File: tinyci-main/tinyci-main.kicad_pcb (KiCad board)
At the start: 2 copper layers, 110 x 82.5 mm, 54 parts, among them J1 Jack-DC, J2 Jack-DC, J3 Jack-DC, J4 Conn_01x13_Male, J5 Conn_01x13_Male, J6 Jack-DC, J7 Jack-DC, J8 Conn_01x06_Male, J9 Conn_01x06_Male, K1 SANYOU_SRD_Form_C, K2 SANYOU_SRD_Form_C, K3 SANYOU_SRD_Form_C, K4 SANYOU_SRD_Form_C, Q1 BC337, Q2 BC337, Q3 BC337, Q4 BC337, U1 AMS1117-3.3

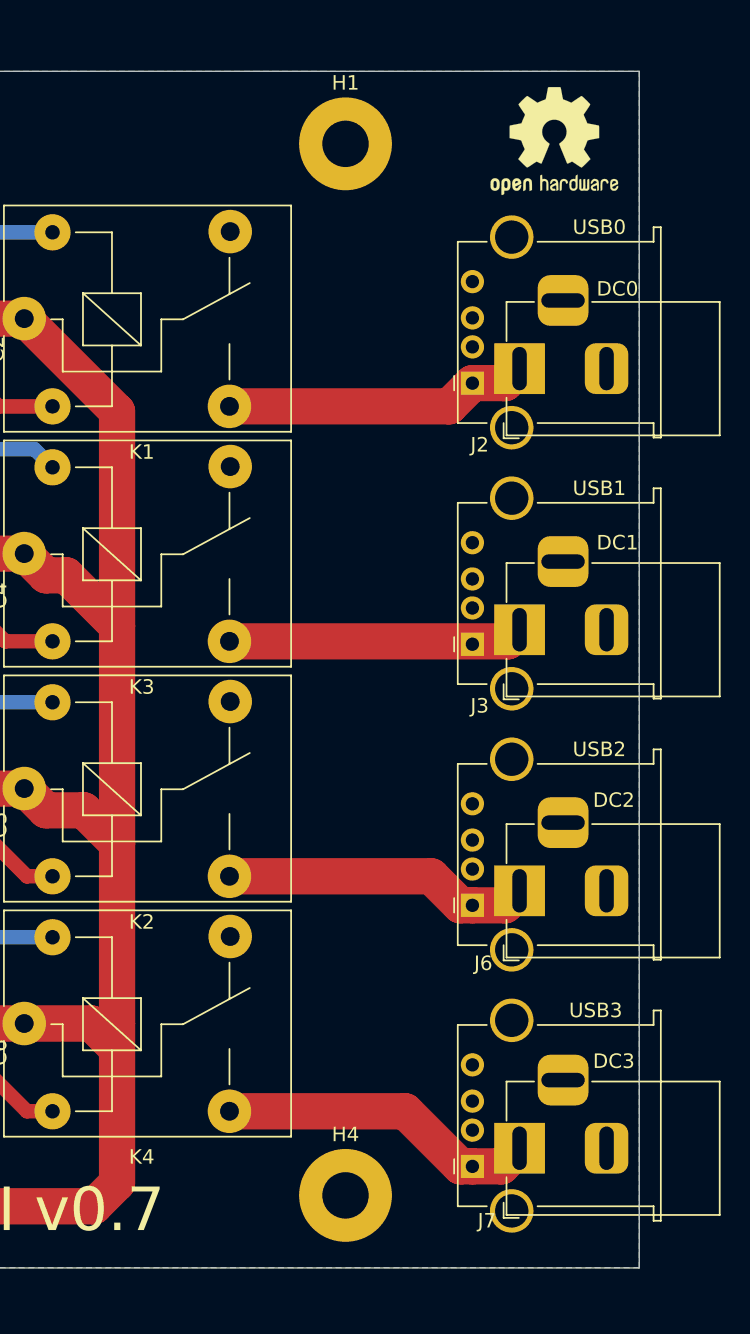
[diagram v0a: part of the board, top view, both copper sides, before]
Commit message: tinyci-main: Replaced the PCB single USB-A connectors by the stacked ones.
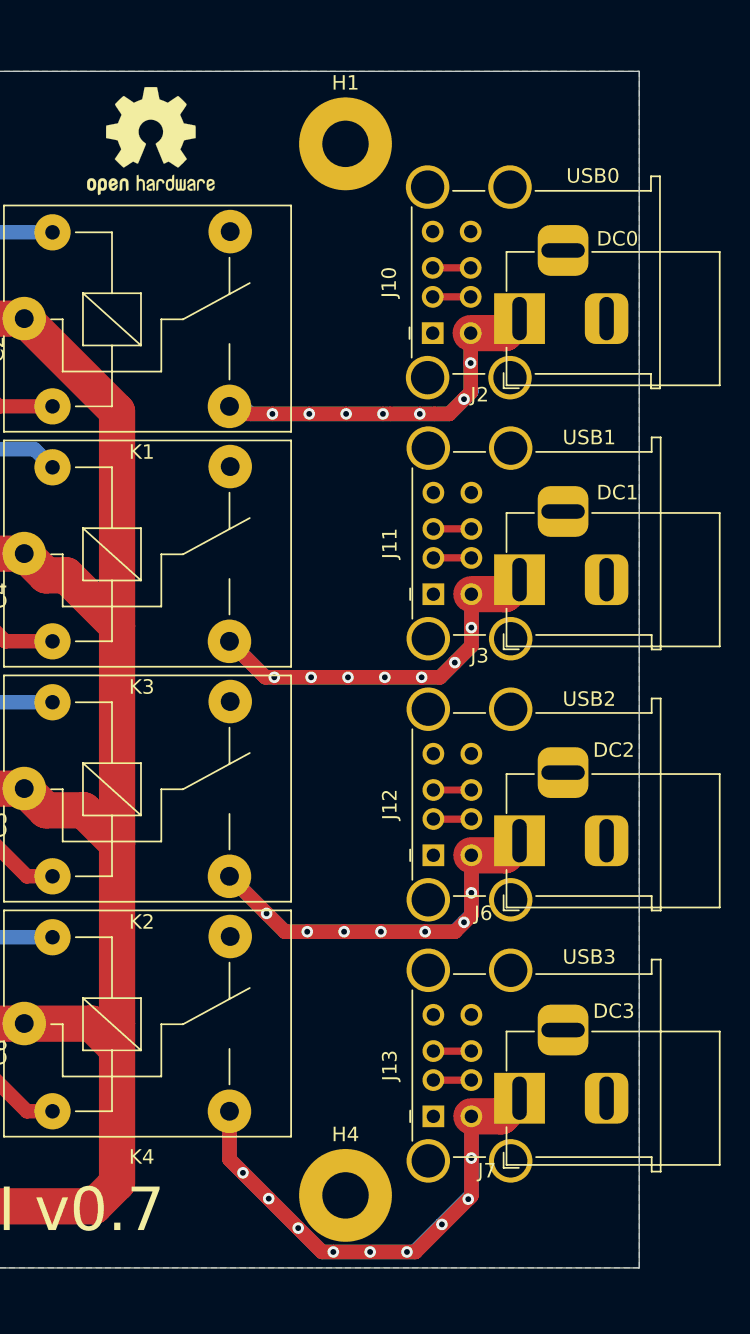
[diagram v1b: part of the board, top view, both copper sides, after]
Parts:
- J10: renamed from USB0; value USB_A_Stewart_SS-52100-001_Horizontal -> USB_A_Stacked; footprint Connector_USB:USB_A_Stewart_SS-52100-001_Horizontal -> Connector_USB:USB_A_Wuerth_61400826021_Horizontal_Stacked
- J11: renamed from USB1; value USB_A_Stewart_SS-52100-001_Horizontal -> USB_A_Stacked; footprint Connector_USB:USB_A_Stewart_SS-52100-001_Horizontal -> Connector_USB:USB_A_Wuerth_61400826021_Horizontal_Stacked
- J12: renamed from USB2; value USB_A_Stewart_SS-52100-001_Horizontal -> USB_A_Stacked; footprint Connector_USB:USB_A_Stewart_SS-52100-001_Horizontal -> Connector_USB:USB_A_Wuerth_61400826021_Horizontal_Stacked
- J13: renamed from USB3; value USB_A_Stewart_SS-52100-001_Horizontal -> USB_A_Stacked; footprint Connector_USB:USB_A_Stewart_SS-52100-001_Horizontal -> Connector_USB:USB_A_Wuerth_61400826021_Horizontal_Stacked
- moved REF** 27.8 mm to (163.8, 52.3)
- moved J10 4.41 mm to (183.3, 65.5)
- moved J11 4.38 mm to (183.3, 83.5)
- moved J12 4.38 mm to (183.3, 101.5)
- moved J13 4.38 mm to (183.3, 119.5)
- moved J2 3.45 mm to (189.2, 64.5)
- moved J3 3.45 mm to (189.2, 82.5)
- moved J6 3.45 mm to (189.2, 100.5)
- moved J7 3.45 mm to (189.2, 118.3)
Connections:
- net +3V3 renamed +3.3V
- J10 pad 1: /NO_1 -> unconnected-(J10-Pad1)
- J10 pad 2: (no net) -> Net-(J10-Pad2)
- J10 pad 3: (no net) -> Net-(J10-Pad3)
- J10 pad 5: GND -> NO_1
- J11 pad 1: /NO_2 -> unconnected-(J11-Pad1)
- J11 pad 2: (no net) -> Net-(J11-Pad2)
- J11 pad 3: (no net) -> Net-(J11-Pad3)
- J11 pad 5: GND -> NO_2
- J12 pad 1: /NO_3 -> unconnected-(J12-Pad1)
- J12 pad 2: (no net) -> Net-(J12-Pad2)
- J12 pad 3: (no net) -> Net-(J12-Pad3)
- J12 pad 5: GND -> NO_3
- J13 pad 1: /NO_4 -> unconnected-(J13-Pad1)
- J13 pad 2: (no net) -> Net-(J13-Pad2)
- J13 pad 3: (no net) -> Net-(J13-Pad3)
- J13 pad 5: GND -> NO_4
- J2 pad 1: /NO_1 -> NO_1
- J3 pad 1: /NO_2 -> NO_2
- J4 pad 12: Net-(J4-Pad12) -> unconnected-(J4-Pad12)
- J4 pad 13: Net-(J4-Pad13) -> unconnected-(J4-Pad13)
- J4 pad 4: Net-(J4-Pad4) -> unconnected-(J4-Pad4)
- J6 pad 1: /NO_3 -> NO_3
- J7 pad 1: /NO_4 -> NO_4
- K1 pad 3: /NO_1 -> NO_1
- K1 pad 4: Net-(K1-Pad4) -> unconnected-(K1-Pad4)
- K2 pad 3: /NO_3 -> NO_3
- K2 pad 4: Net-(K2-Pad4) -> unconnected-(K2-Pad4)
- K3 pad 3: /NO_2 -> NO_2
- K3 pad 4: Net-(K3-Pad4) -> unconnected-(K3-Pad4)
- K4 pad 3: /NO_4 -> NO_4
- K4 pad 4: Net-(K4-Pad4) -> unconnected-(K4-Pad4)
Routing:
- net NO_4: track 0.00 -> 63.3 mm, vias 0 -> 9
- net NO_3: track 0.00 -> 49.5 mm, vias 0 -> 7
- net NO_2: track 0.00 -> 48.1 mm, vias 0 -> 7
- net NO_1: track 0.00 -> 46.9 mm, vias 0 -> 7
- net /NO_4: track 22.1 -> 0.00 mm
- net /NO_3: track 21.2 -> 0.00 mm
- net /NO_1: track 21.1 -> 0.00 mm
- net /NO_2: track 20.3 -> 0.00 mm
- net Net-(J13-Pad3): track 0.00 -> 2.62 mm
- net Net-(J13-Pad2): track 0.00 -> 2.62 mm
- net Net-(J12-Pad3): track 0.00 -> 2.62 mm
- net Net-(J12-Pad2): track 0.00 -> 2.62 mm
- net Net-(J11-Pad3): track 0.00 -> 2.62 mm
- net Net-(J11-Pad2): track 0.00 -> 2.62 mm
- net Net-(J10-Pad3): track 0.00 -> 2.62 mm
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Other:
- board text added: "USB0"
- board text added: "USB1"
- board text added: "USB2"
- board text added: "USB3"

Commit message: tinyci-main: Bumped version to 0.8.
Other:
- board text added: "TinyCI v0.8"
- board text added: "TinyCI v0.8 http://github.com/superna9999/tinyci CERN OPEN HARDWARE LICENCE v1.1"
- board text removed: "TinyCI v0.7"
- board text removed: "TinyCI v0.7 http://github.com/superna9999/tinyci CERN OPEN HARDWARE LICENCE v1.1"
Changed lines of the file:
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@@
   (gr_line (start 197.5 130) (end 87.5 130) (layer "Edge.Cuts") (width 0.05))
   (gr_line (start 197.5 47.5) (end 197.5 130) (layer "Edge.Cuts") (width 0.05))
-  (gr_text "TinyCI v0.7\nhttp://github.com/superna9999/tinyci\n\nCERN OPEN HARDWARE LICENCE v1.1" (at 110.9 85.05 90) (layer "B.SilkS")
+  (gr_text "TinyCI v0.8\nhttp://github.com/superna9999/tinyci\n\nCERN OPEN HARDWARE LICENCE v1.1" (at 110.9 85.05 90) (layer "B.SilkS")
     (effects (font (size 3 2.5) (thickness 0.5)) (justify mirror))
   )
@@
     (effects (font (size 1 1) (thickness 0.15)))
   )
-  (gr_text "TinyCI v0.7" (at 153.25 126) (layer "F.SilkS")
+  (gr_text "TinyCI v0.8" (at 153.25 126) (layer "F.SilkS")
     (effects (font (size 3 3) (thickness 0.5)))
   )

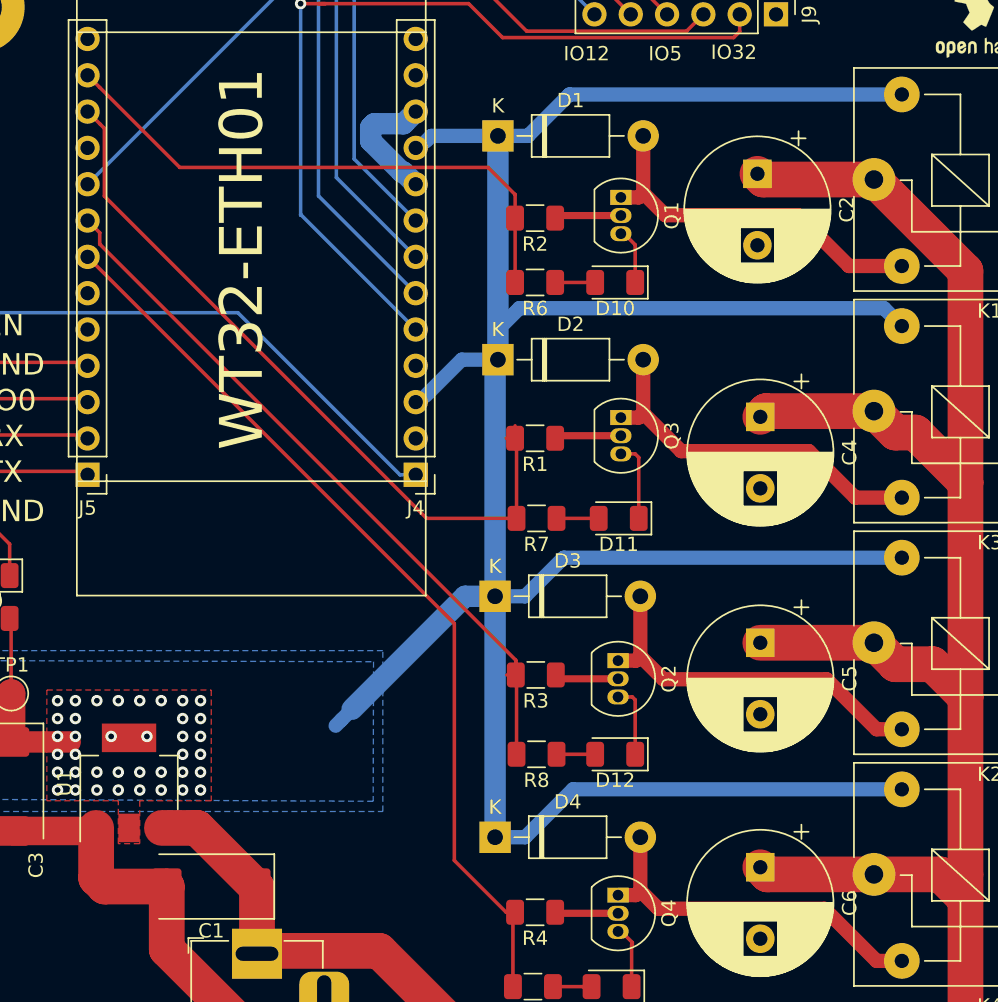
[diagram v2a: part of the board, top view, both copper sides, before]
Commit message: tinyci-main: Replaced the relay coil flyback diodes by SMD parts to speed up the board assembly.
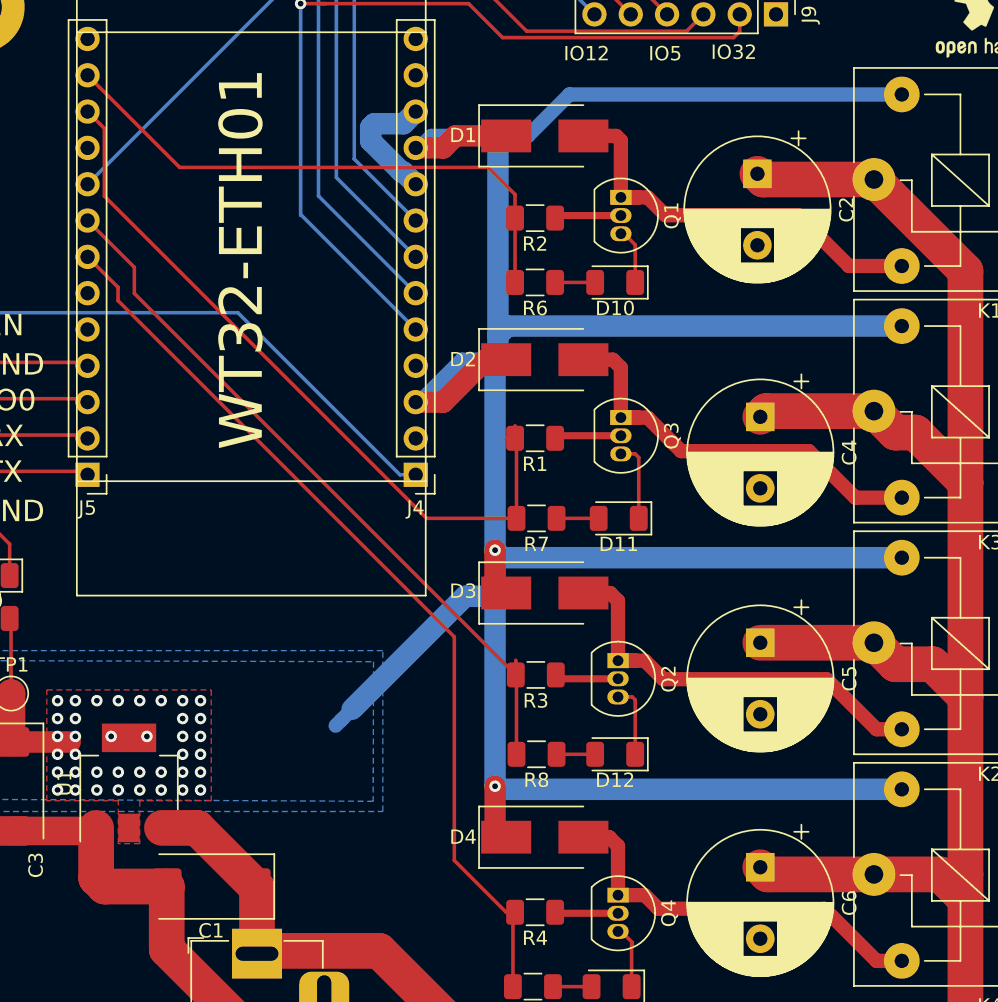
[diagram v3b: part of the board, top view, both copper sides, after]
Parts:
- D1, D2, D3, D4: value 1N4001 -> S1BB-13-F; footprint Diode_THT:D_DO-41_SOD81_P10.16mm_Horizontal -> Diode_SMD:D_SMB_Handsoldering
- moved D3 3.49 mm to (132.1, 93.5)
- moved D4 3.48 mm to (132.1, 110.5)
- moved D1 3.28 mm to (132.1, 61.5)
- moved D2 3.28 mm to (132.1, 77.2)
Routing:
- net +3.3V: track 209.7 -> 224.5 mm, vias 38 -> 40
- net /COIL_1_1: track 25.9 -> 29.6 mm
- net /COIL_1_3: track 26.3 -> 29.9 mm
- net /COIL_1_2: track 26.0 -> 29.6 mm
- net /COIL_1_4: track 25.8 -> 27.9 mm

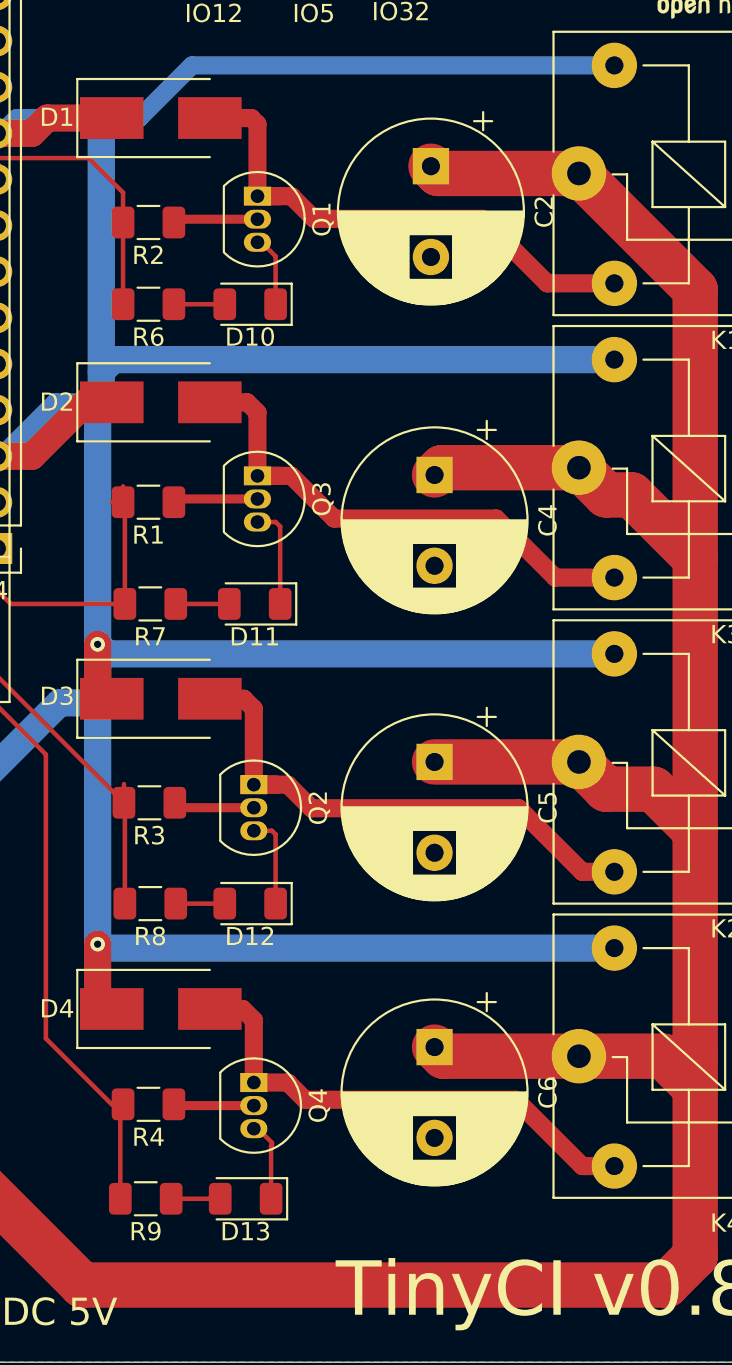
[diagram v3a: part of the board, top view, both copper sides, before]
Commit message: tinyci-main: Replaced the relay coil transistors by SMD parts to speed up the board assembly.
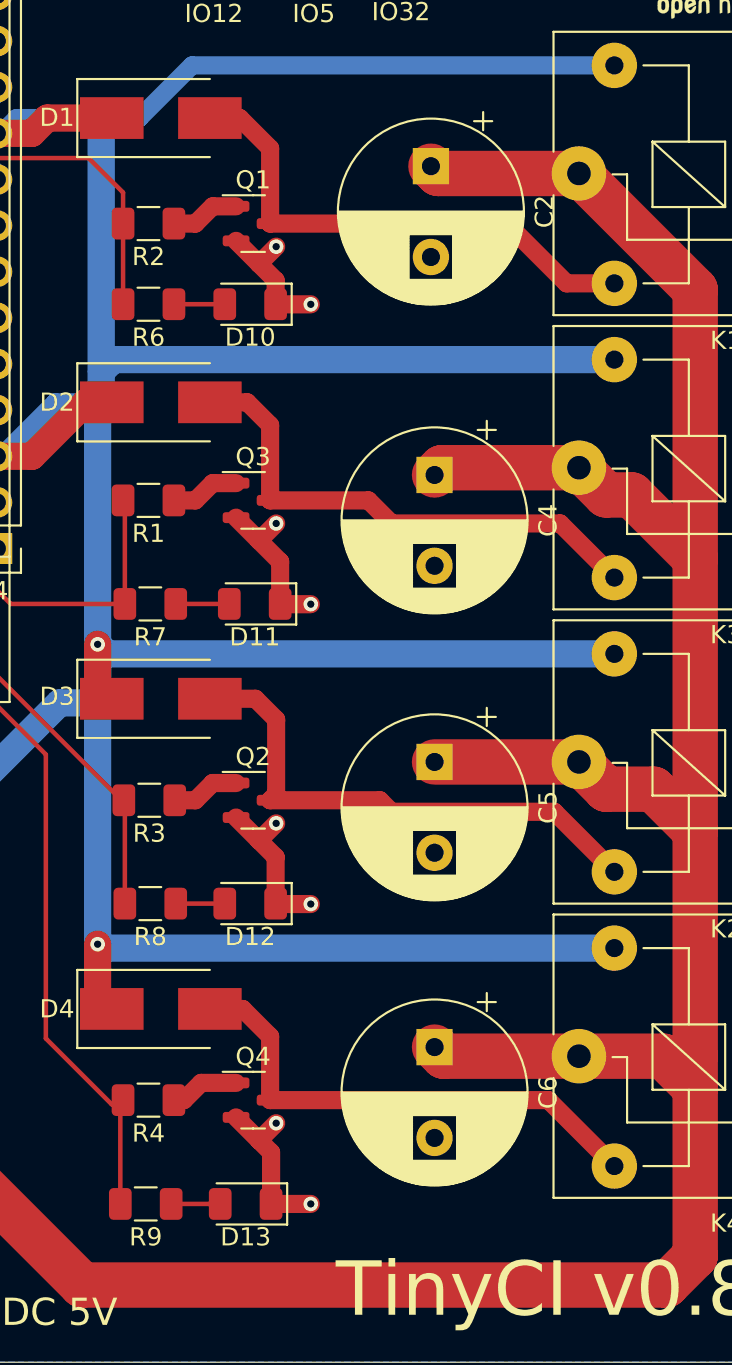
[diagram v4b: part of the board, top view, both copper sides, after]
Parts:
- Q1, Q2, Q3, Q4: value BC337 -> BC817-25; footprint Package_TO_SOT_THT:TO-92_Inline -> Package_TO_SOT_SMD:SOT-23
- moved Q1 1.53 mm to (137.2, 67.3), turned to 0 degrees
- moved Q3 1.37 mm to (137.2, 82.5), turned to 0 degrees
- moved Q4 0.97 mm to (137.2, 115.6), turned to 0 degrees
- moved Q2 0.86 mm to (137.2, 99.1), turned to 0 degrees
- moved D13 0.28 mm to (136.8, 121.3)
- moved R9 0.28 mm to (131.2, 121.3)
- moved R4 0.23 mm to (131.4, 115.6)
- moved R3 0.14 mm to (131.4, 99.1)
- moved R1 0.10 mm to (131.4, 82.5)
- moved R2 0.06 mm to (131.4, 67.3)
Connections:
- Q1 pad 1: /COIL_1_1 -> Net-(Q1-Pad1)
- Q1 pad 2: Net-(Q1-Pad2) -> GND
- Q1 pad 3: GND -> /COIL_1_1
- Q2 pad 1: /COIL_1_3 -> Net-(Q2-Pad1)
- Q2 pad 2: Net-(Q2-Pad2) -> GND
- Q2 pad 3: GND -> /COIL_1_3
- Q3 pad 1: /COIL_1_2 -> Net-(Q3-Pad1)
- Q3 pad 2: Net-(Q3-Pad2) -> GND
- Q3 pad 3: GND -> /COIL_1_2
- Q4 pad 1: /COIL_1_4 -> Net-(Q4-Pad1)
- Q4 pad 2: Net-(Q4-Pad2) -> GND
- Q4 pad 3: GND -> /COIL_1_4
- R1 pad 1: Net-(Q3-Pad2) -> Net-(Q3-Pad1)
- R2 pad 1: Net-(Q1-Pad2) -> Net-(Q1-Pad1)
- R3 pad 1: Net-(Q2-Pad2) -> Net-(Q2-Pad1)
- R4 pad 1: Net-(Q4-Pad2) -> Net-(Q4-Pad1)
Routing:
- net GND: track 75.6 -> 91.0 mm, vias 0 -> 8
- net Net-(Q3-Pad2): track 4.67 -> 0.00 mm
- net Net-(Q1-Pad2): track 4.67 -> 0.00 mm
- net Net-(Q2-Pad2): track 4.46 -> 0.00 mm
- net Net-(Q4-Pad2): track 4.43 -> 0.00 mm
- net Net-(Q4-Pad1): track 0.00 -> 3.91 mm
- net Net-(Q3-Pad1): track 0.00 -> 3.82 mm
- net Net-(Q1-Pad1): track 0.00 -> 3.82 mm
- net Net-(Q2-Pad1): track 0.00 -> 3.77 mm
- net /IO14: track 51.7 -> 49.8 mm
- net /IO4: track 51.7 -> 50.2 mm
- net /COIL_1_1: track 29.6 -> 28.5 mm
- net /COIL_1_2: track 29.6 -> 28.7 mm
- net /COIL_1_3: track 29.9 -> 29.3 mm

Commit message: tinyci-main: Bumped version to 0.9.
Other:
- board text added: "TinyCI v0.9"
- board text added: "TinyCI v0.9 http://github.com/superna9999/tinyci CERN OPEN HARDWARE LICENCE v1.1"
- board text removed: "TinyCI v0.8"
- board text removed: "TinyCI v0.8 http://github.com/superna9999/tinyci CERN OPEN HARDWARE LICENCE v1.1"
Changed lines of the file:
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@@
   (gr_line (start 197.5 130) (end 87.5 130) (layer "Edge.Cuts") (width 0.05))
   (gr_line (start 197.5 47.5) (end 197.5 130) (layer "Edge.Cuts") (width 0.05))
-  (gr_text "TinyCI v0.8\nhttp://github.com/superna9999/tinyci\n\nCERN OPEN HARDWARE LICENCE v1.1" (at 110.9 85.05 90) (layer "B.SilkS")
+  (gr_text "TinyCI v0.9\nhttp://github.com/superna9999/tinyci\n\nCERN OPEN HARDWARE LICENCE v1.1" (at 110.9 85.05 90) (layer "B.SilkS")
     (effects (font (size 3 2.5) (thickness 0.5)) (justify mirror))
   )
@@
     (effects (font (size 1 1) (thickness 0.15)))
   )
-  (gr_text "TinyCI v0.8" (at 153.25 126) (layer "F.SilkS")
+  (gr_text "TinyCI v0.9" (at 153.25 126) (layer "F.SilkS")
     (effects (font (size 3 3) (thickness 0.5)))
   )
